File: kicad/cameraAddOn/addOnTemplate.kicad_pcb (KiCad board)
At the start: 2 copper layers, 97.4 x 53.3 mm, 84 parts, among them J1 USB_B_Micro, J11 Conn_01x08, J12 USB_B, J2 Conn_02x09_Odd_Even, J3 GTFP08431BEU, J4 HDMI_A, J5 Conn_01x08, J6 Conn_02x18_Odd_Even, J7 Conn_01x08, J8 Conn_01x08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

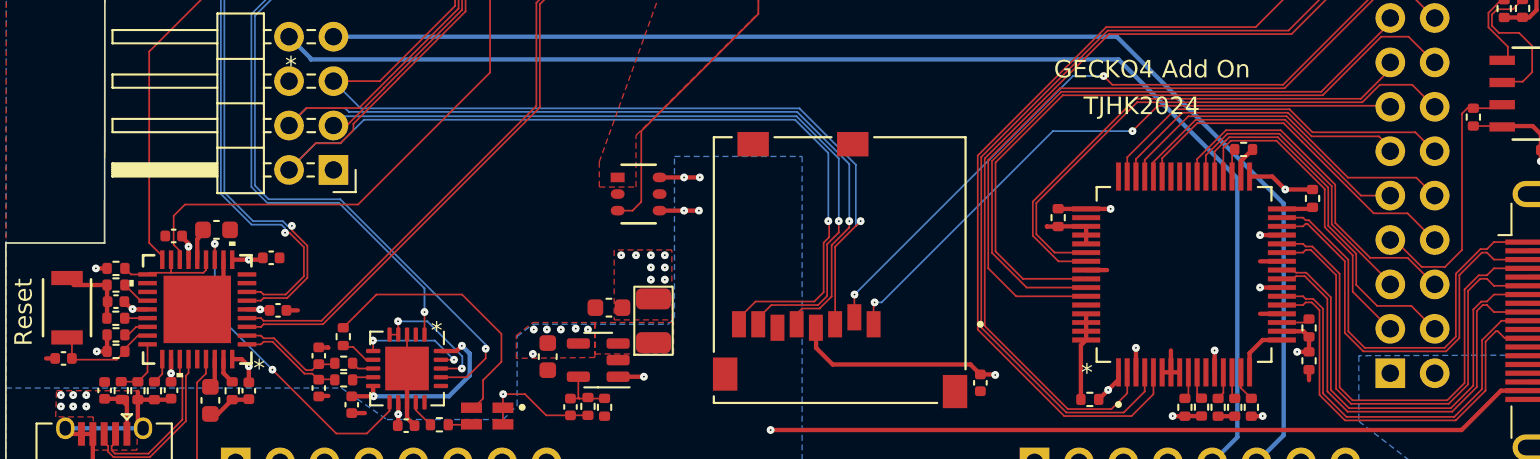
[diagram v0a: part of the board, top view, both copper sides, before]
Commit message: V1.1 of perifAddOn (added bus-switch on sd-card)
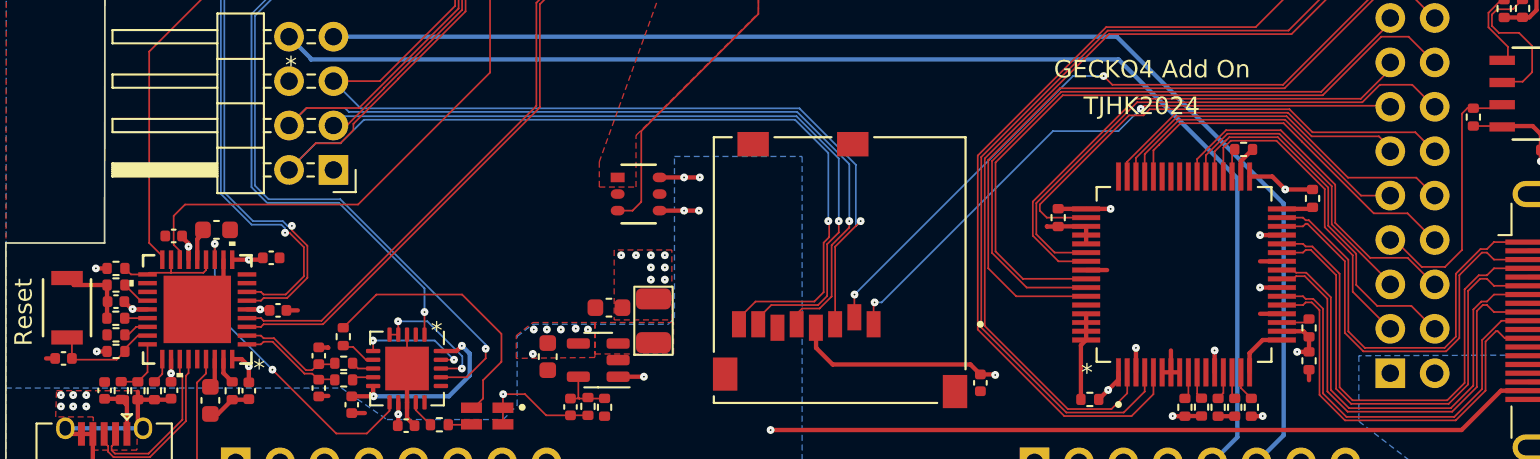
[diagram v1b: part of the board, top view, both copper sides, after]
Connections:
- R15 pad 1: +3.3V -> GND
- U7 pad 43: HDMI_Green4 -> GND
- U7 pad 44: HDMI_Green3 -> HDMI_Green4
- U7 pad 45: HDMI_Green2 -> HDMI_Green3
- U7 pad 46: HDMI_Green1 -> HDMI_Green2
- U7 pad 47: HDMI_Green0 -> HDMI_Green1
- U7 pad 50: GND -> HDMI_Green0
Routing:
- net HDMI_Green0: track 20.8 -> 29.0 mm
- net +3.3V: track 71.2 -> 70.2 mm
- net HDMI_Green4: track 20.2 -> 21.0 mm
- net HDMI_Green3: track 17.2 -> 17.9 mm
- net HDMI_Green2: track 20.4 -> 21.0 mm
